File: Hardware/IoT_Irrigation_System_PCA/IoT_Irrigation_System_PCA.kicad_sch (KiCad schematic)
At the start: 21 parts, among them J1 Conn_01x19_Socket, J2 Conn_01x19_Socket, J3 Conn_01x04_Socket, J4 691137710002, J5 691137710002, J6 691137710002, J7 Jack-DC, J8 Conn_01x01, J9 Conn_01x01, Q1 IRLZ34N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

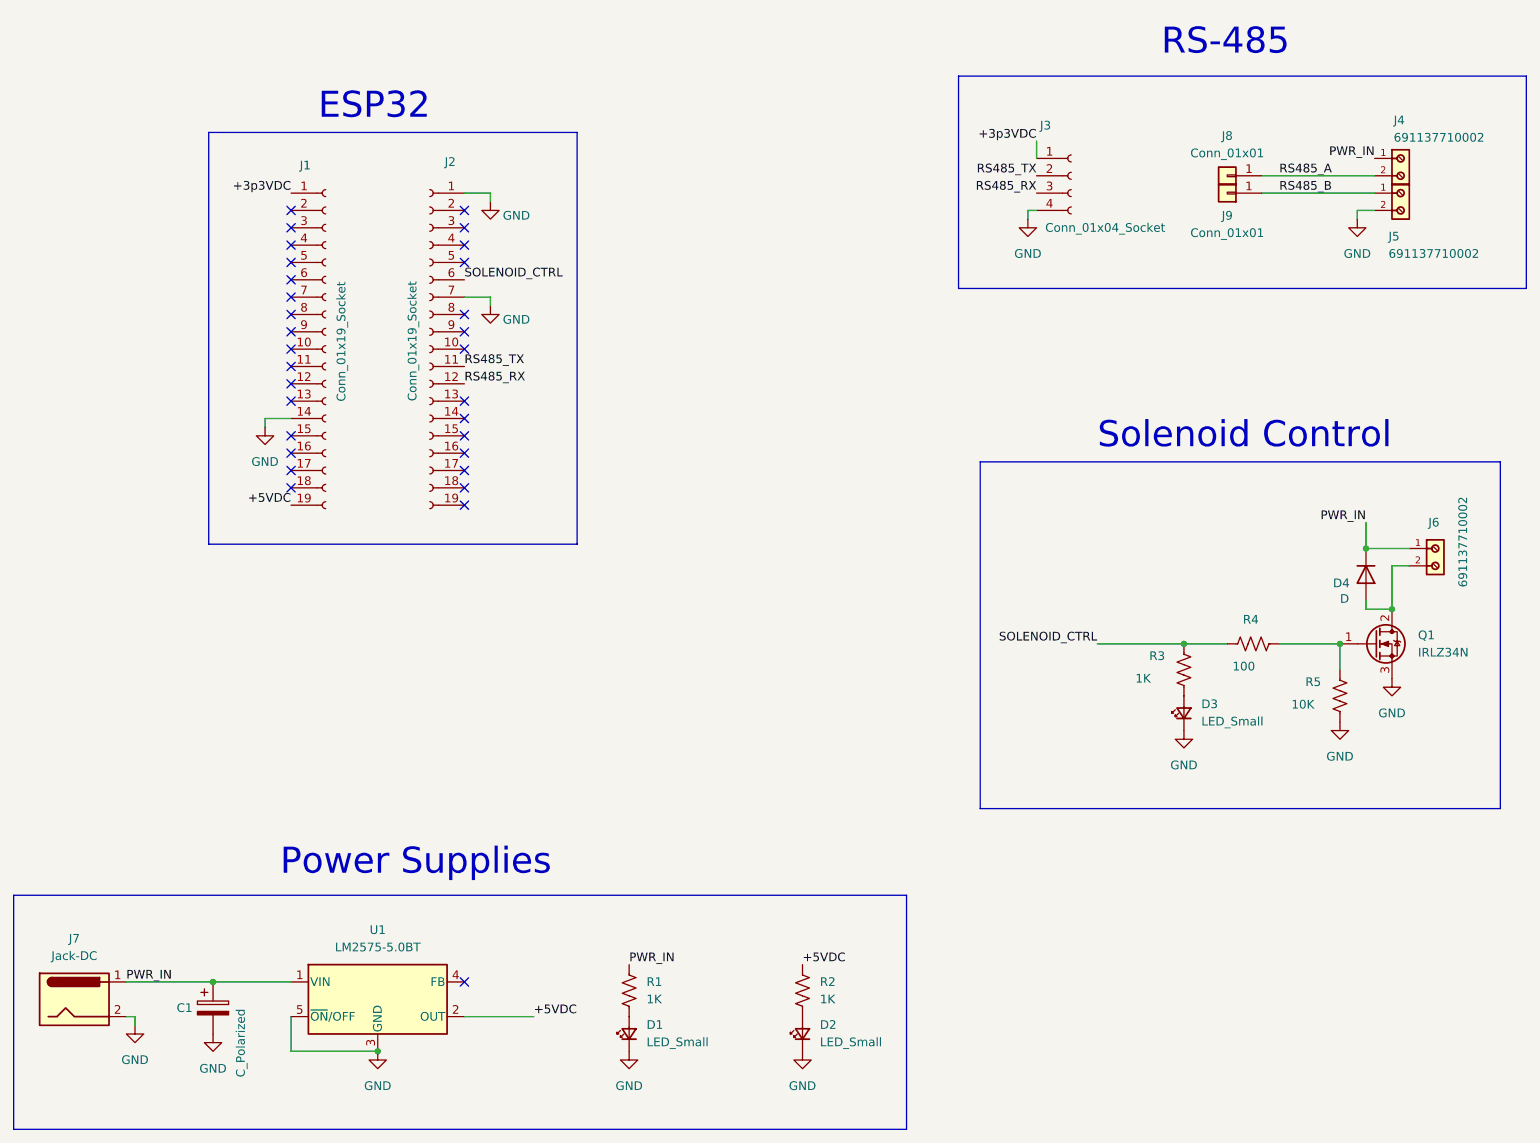
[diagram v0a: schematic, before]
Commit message: 1. Added Wifi connectivity logic 2. Fixed error in getSettings() tries loop 3. Modified TB delay to 180s (3 min) 4. Updates to PCB design
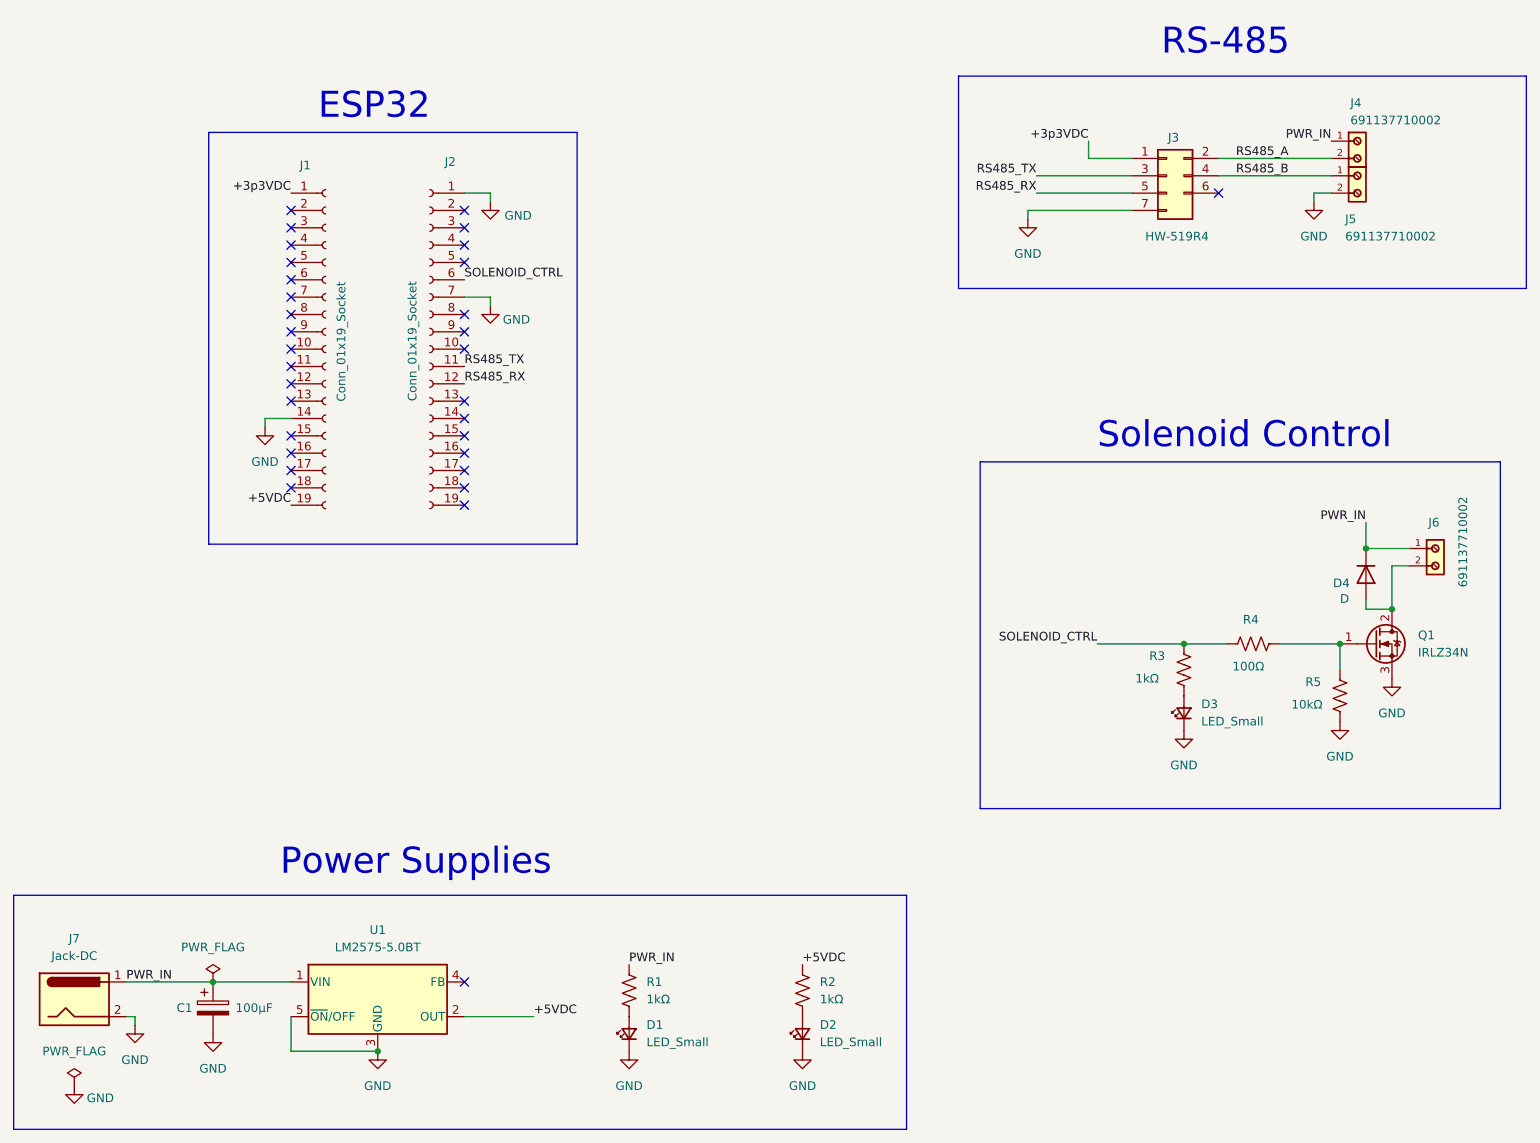
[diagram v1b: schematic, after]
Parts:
- removed J3: Conn_01x04_Socket, Connector_PinSocket_2.54mm:PinSocket_1x04_P2.54mm_Vertical, symbol Connector:Conn_01x04_Socket
- removed J8, J9: Conn_01x01, symbol Connector_Generic:Conn_01x01
- added J3: HW-519R4, RS485_Module:HW-519R4, symbol Connector_Generic:Conn_2Rows-07Pins
- C1: value C_Polarized -> 100µF; footprint Capacitor_THT:CP_Radial_D5.0mm_P2.50mm -> Capacitor_THT:CP_Radial_D8.0mm_P3.80mm
- R1, R2, R3: value 1K -> 1kΩ; footprint Resistor_THT:R_Axial_DIN0207_L6.3mm_D2.5mm_P7.62mm_Horizontal -> Resistor_THT:R_Axial_DIN0207_L6.3mm_D2.5mm_P10.16mm_Horizontal
- R4: value 100 -> 100Ω; footprint Resistor_THT:R_Axial_DIN0207_L6.3mm_D2.5mm_P7.62mm_Horizontal -> Resistor_THT:R_Axial_DIN0207_L6.3mm_D2.5mm_P10.16mm_Horizontal
- R5: value 10K -> 10kΩ; footprint Resistor_THT:R_Axial_DIN0207_L6.3mm_D2.5mm_P7.62mm_Horizontal -> Resistor_THT:R_Axial_DIN0207_L6.3mm_D2.5mm_P10.16mm_Horizontal
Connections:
- net +3p3VDC: now also J3.1 (Pin_1)
- net GND: now also J3.7 (Pin_7)
- net RS485_A: now also J3.2 (Pin_2)
- net RS485_B: now also J3.4 (Pin_4)
- net RS485_RX: now also J3.5 (Pin_5)
- net RS485_TX: now also J3.3 (Pin_3)
- no-connect marks 31 -> 32
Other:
- moved on the sheet: J4, J5

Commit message: Updated PCB
Spaced ESP32 socket headers to 25.4mm
Moved RS485 and power supply components
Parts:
- D1, D2, D3: footprint LED_THT:LED_D3.0mm_Horizontal_O1.27mm_Z2.0mm -> LED_THT:LED_D3.0mm
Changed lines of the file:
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@@
 			)
 		)
-		(property "Footprint" "LED_THT:LED_D3.0mm_Horizontal_O1.27mm_Z2.0mm"
+		(property "Footprint" "LED_THT:LED_D3.0mm"
 			(at 201.93 127 90)
 			(effects
@@
 			)
 		)
-		(property "Footprint" "LED_THT:LED_D3.0mm_Horizontal_O1.27mm_Z2.0mm"
+		(property "Footprint" "LED_THT:LED_D3.0mm"
 			(at 146.05 173.99 90)
 			(effects
@@
 			)
 		)
-		(property "Footprint" "LED_THT:LED_D3.0mm_Horizontal_O1.27mm_Z2.0mm"
+		(property "Footprint" "LED_THT:LED_D3.0mm"
 			(at 120.65 173.99 90)
 			(effects
